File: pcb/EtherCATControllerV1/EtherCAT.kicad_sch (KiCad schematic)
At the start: 6 parts, among them U7 LAN9252/ML

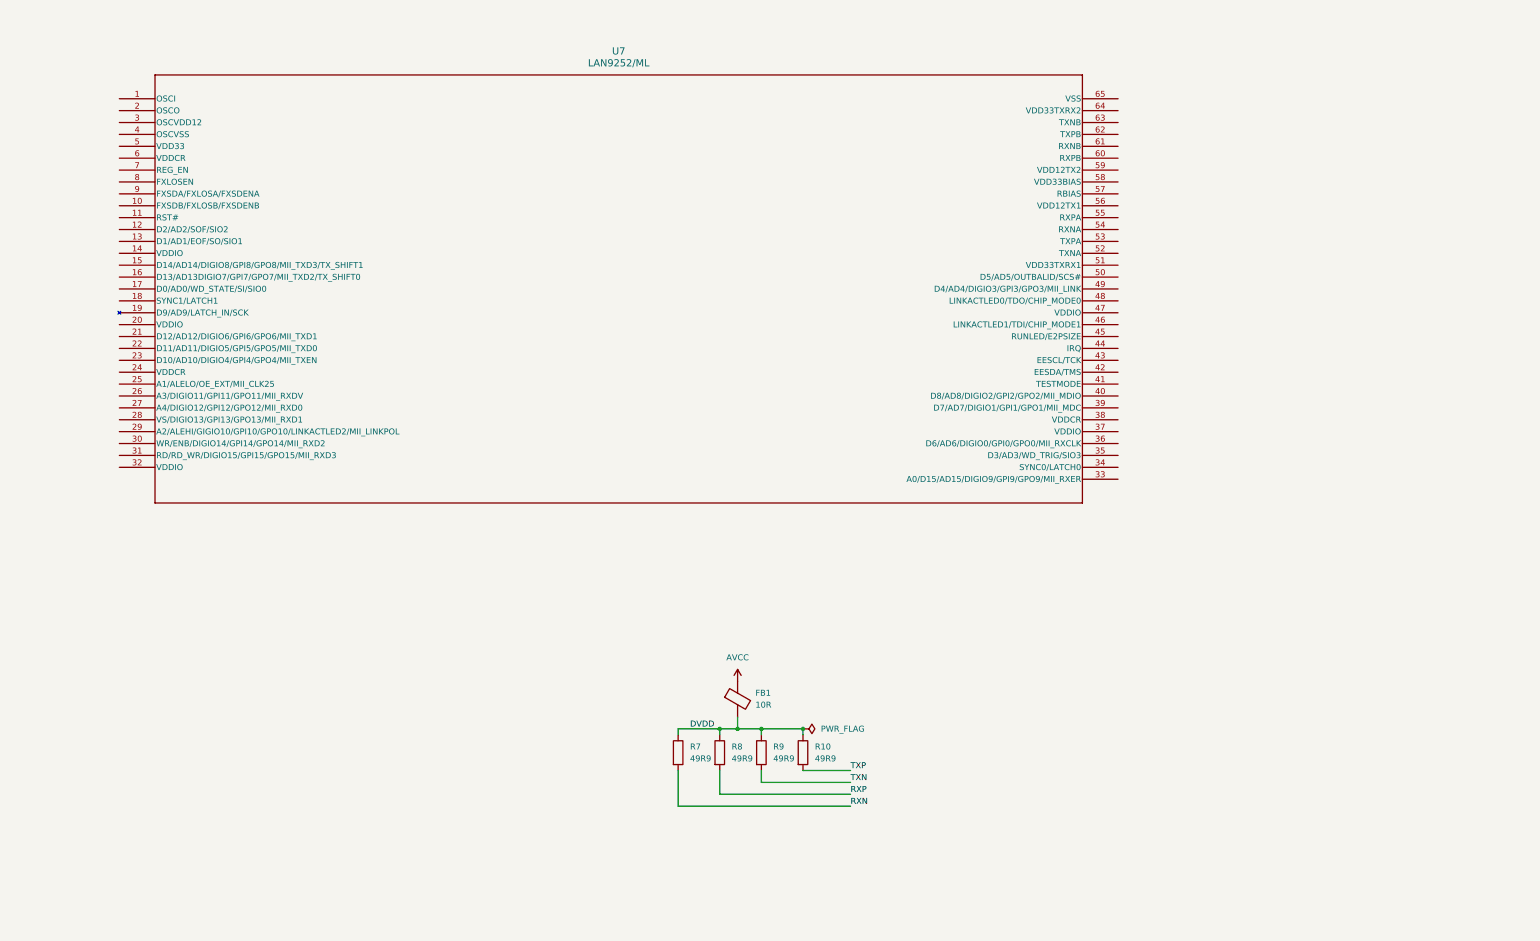
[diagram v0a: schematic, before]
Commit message: Initial design without Ethernet connectors
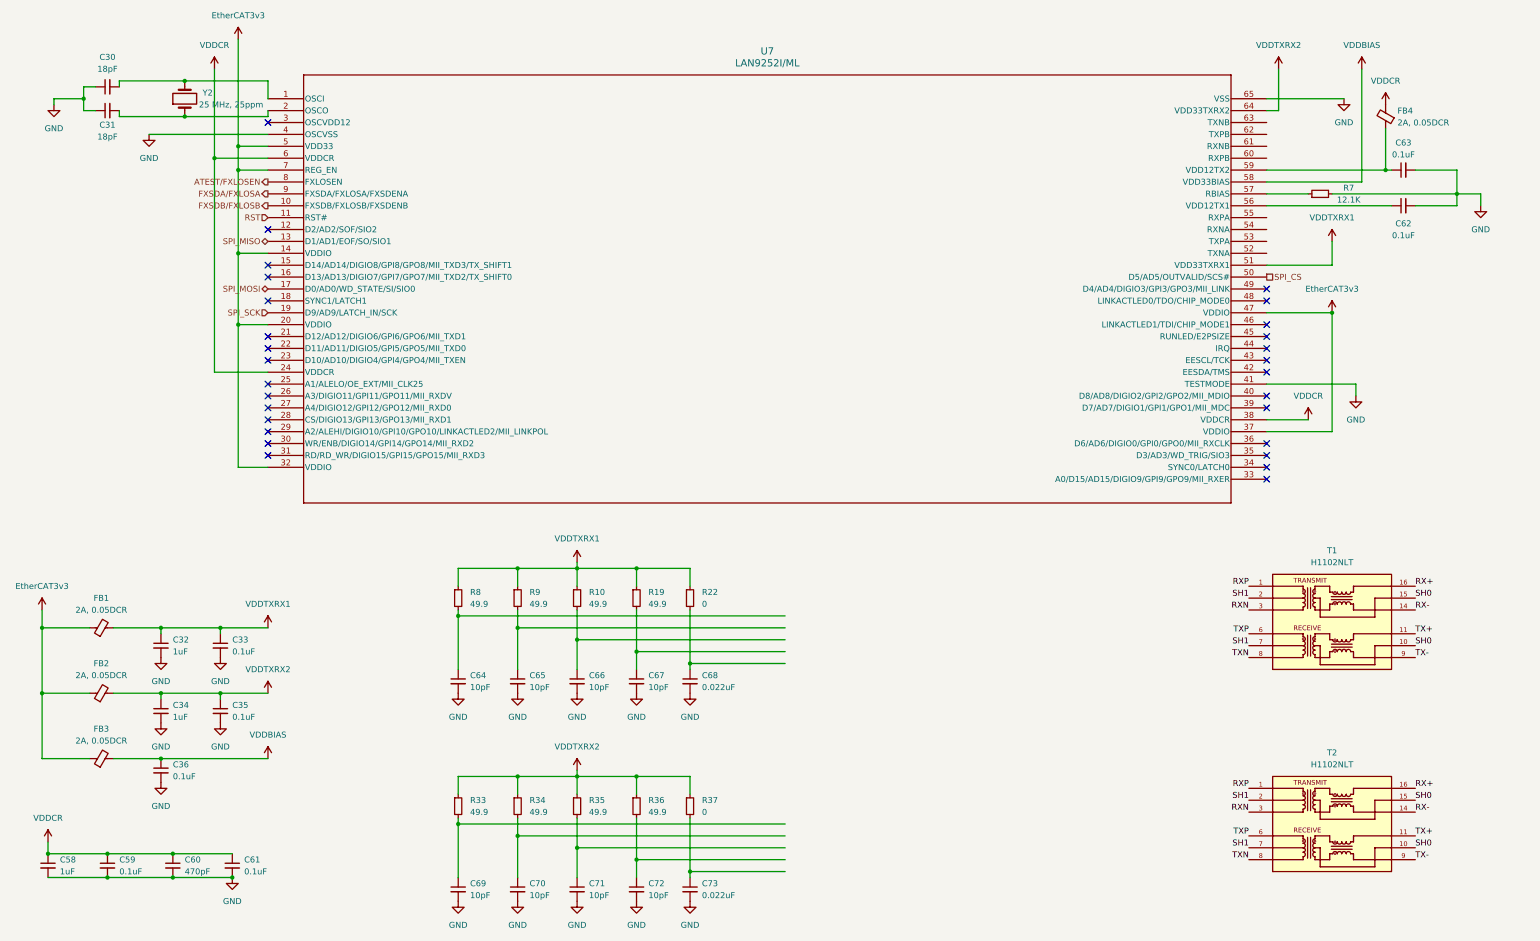
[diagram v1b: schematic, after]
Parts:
- removed FB1: 10R, Inductor_SMD:L_0402_1005Metric, symbol Device:FerriteBead
- removed R10, R7, R8, R9: 49R9, Resistor_SMD:R_0402_1005Metric, symbol Device:R
- removed U7: LAN9252/ML, QFN64_ML_MCH, symbol 2024-06-30_23-12-06:LAN9252_ML
- added C30, C31: 18pF, symbol Device:C_Small
- added C32, C34, C58: 1uF, symbol Device:C_Small
- added C33, C35, C36, C59, C61, C62, C63: 0.1uF, symbol Device:C_Small
- added C60: 470pF, symbol Device:C_Small
- added C64, C65, C66, C67, C69, C70, C71, C72: 10pF, symbol Device:C_Small
- added C68, C73: 0.022uF, symbol Device:C_Small
- added FB1, FB2, FB3, FB4: 2A, 0.05DCR, symbol Device:FerriteBead_Small
- added R10, R19, R33, R34, R35, R36, R8, R9: 49.9, symbol Device:R_Small
- added R22, R37: 0, symbol Device:R_Small
- added R7: 12.1K, symbol Device:R_Small
- added T1, T2: H1102NLT, Ethernet:XFMR_H1102NLT, symbol H1102NLT:H1102NLT
- added U7: LAN9252I/ML, QFN64_ML_MCH, symbol 2024-07-01_21-03-15:LAN9252I_ML
- added Y2: 25 MHz, 25ppm, symbol Device:Crystal
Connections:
- net RXN: now also T1.3, T2.3
- net RXP: now also T1.1, T2.1
- net TXN: now also T1.8, T2.8
- net TXP: now also T1.6, T2.6
- new net: C71.1, R35.2
- new net: C30.2, U7.1 (OSCI), Y2.2
- new net: C31.2, U7.2 (OSCO), Y2.1
- new net: C62.1, U7.56 (VDD12TX1)
- new net: R7.1, U7.57 (RBIAS)
- new net: C63.1, FB4.1, U7.59 (VDD12TX2)
- new net: C70.1, R34.2
- new net: C67.1, R19.2
- new net: C68.1, R22.2
- new net: C66.1, R10.2
- new net: C69.1, R33.2
- new net: C64.1, R8.2
- new net: C72.1, R36.2
- new net: C73.1, R37.2
- new net: C65.1, R9.2
- new net ATEST/FXLOSEN: U7.8 (FXLOSEN)
- new net EtherCAT3v3: FB1.1, FB2.1, FB3.1, U7.14 (VDDIO), U7.20 (VDDIO), U7.32 (VDDIO), U7.37 (VDDIO), U7.47 (VDDIO), U7.5 (VDD33), U7.7 (REG_EN)
- new net FXSDA/FXLOSA: U7.9 (FXSDA/FXLOSA/FXSDENA)
- new net FXSDB/FXLOSB: U7.10 (FXSDB/FXLOSB/FXSDENB)
- new net GND: C30.1, C31.1, C32.2, C33.2, C34.2, C35.2, C36.2, C58.2, C59.2, C60.2, C61.2, C62.2, C63.2, C64.2, C65.2, C66.2, C67.2, C68.2, C69.2, C70.2, C71.2, C72.2, C73.2, R7.2, U7.4 (OSCVSS), U7.41 (TESTMODE), U7.65 (VSS)
- new net RST: U7.11 (RST#)
- new net RX+: T1.16, T2.16
- new net RX-: T1.14, T2.14
- new net SH0: T1.10, T1.15, T2.10, T2.15
- new net SH1: T1.2, T1.7, T2.2, T2.7
- new net SPI_CS: U7.50 (D5/AD5/OUTVALID/SCS#)
- new net SPI_MISO: U7.13 (D1/AD1/EOF/SO/SIO1)
- new net SPI_MOSI: U7.17 (D0/AD0/WD_STATE/SI/SIO0)
- new net SPI_SCK: U7.19 (D9/AD9/LATCH_IN/SCK)
- new net TX+: T1.11, T2.11
- new net TX-: T1.9, T2.9
- new net VDDBIAS: C36.1, FB3.2, U7.58 (VDD33BIAS)
- new net VDDCR: C58.1, C59.1, C60.1, C61.1, FB4.2, U7.24 (VDDCR), U7.38 (VDDCR), U7.6 (VDDCR)
- new net VDDTXRX1: C32.1, C33.1, FB1.2, R10.1, R19.1, R22.1, R8.1, R9.1, U7.51 (VDD33TXRX1)
- new net VDDTXRX2: C34.1, C35.1, FB2.2, R33.1, R34.1, R35.1, R36.1, R37.1, U7.64 (VDD33TXRX2)
- no-connect marks 0 -> 28

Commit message: Added IO Board project
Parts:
- removed T1, T2: H1102NLT, Ethernet:XFMR_H1102NLT, symbol H1102NLT:H1102NLT
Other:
- note added: "EEPROM"

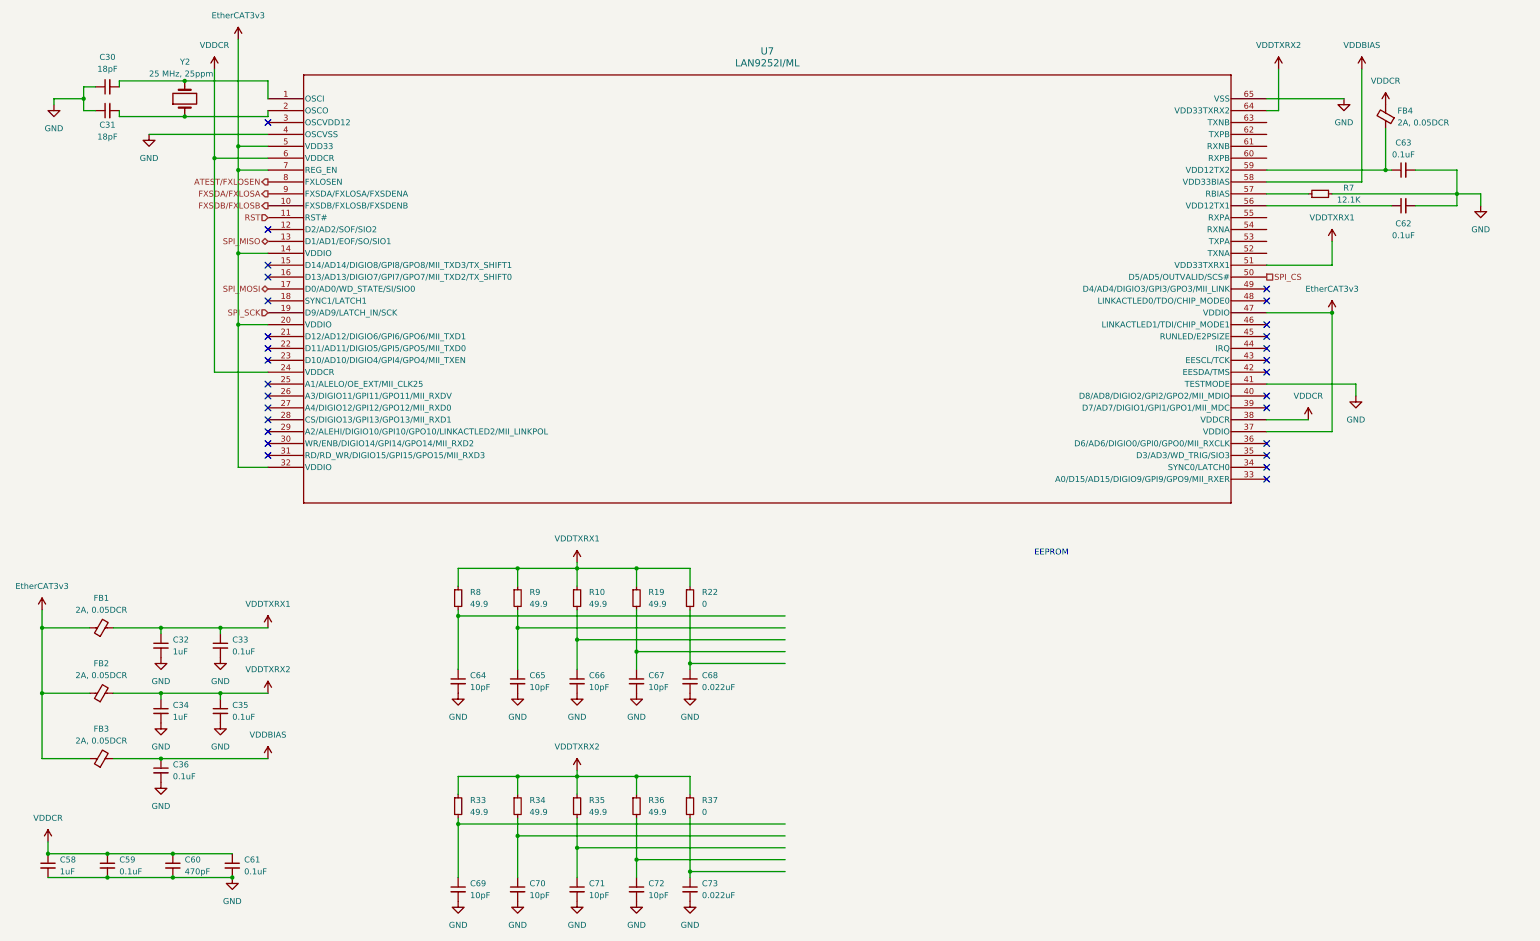
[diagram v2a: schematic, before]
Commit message: schematic finished, need to set proper ERCs
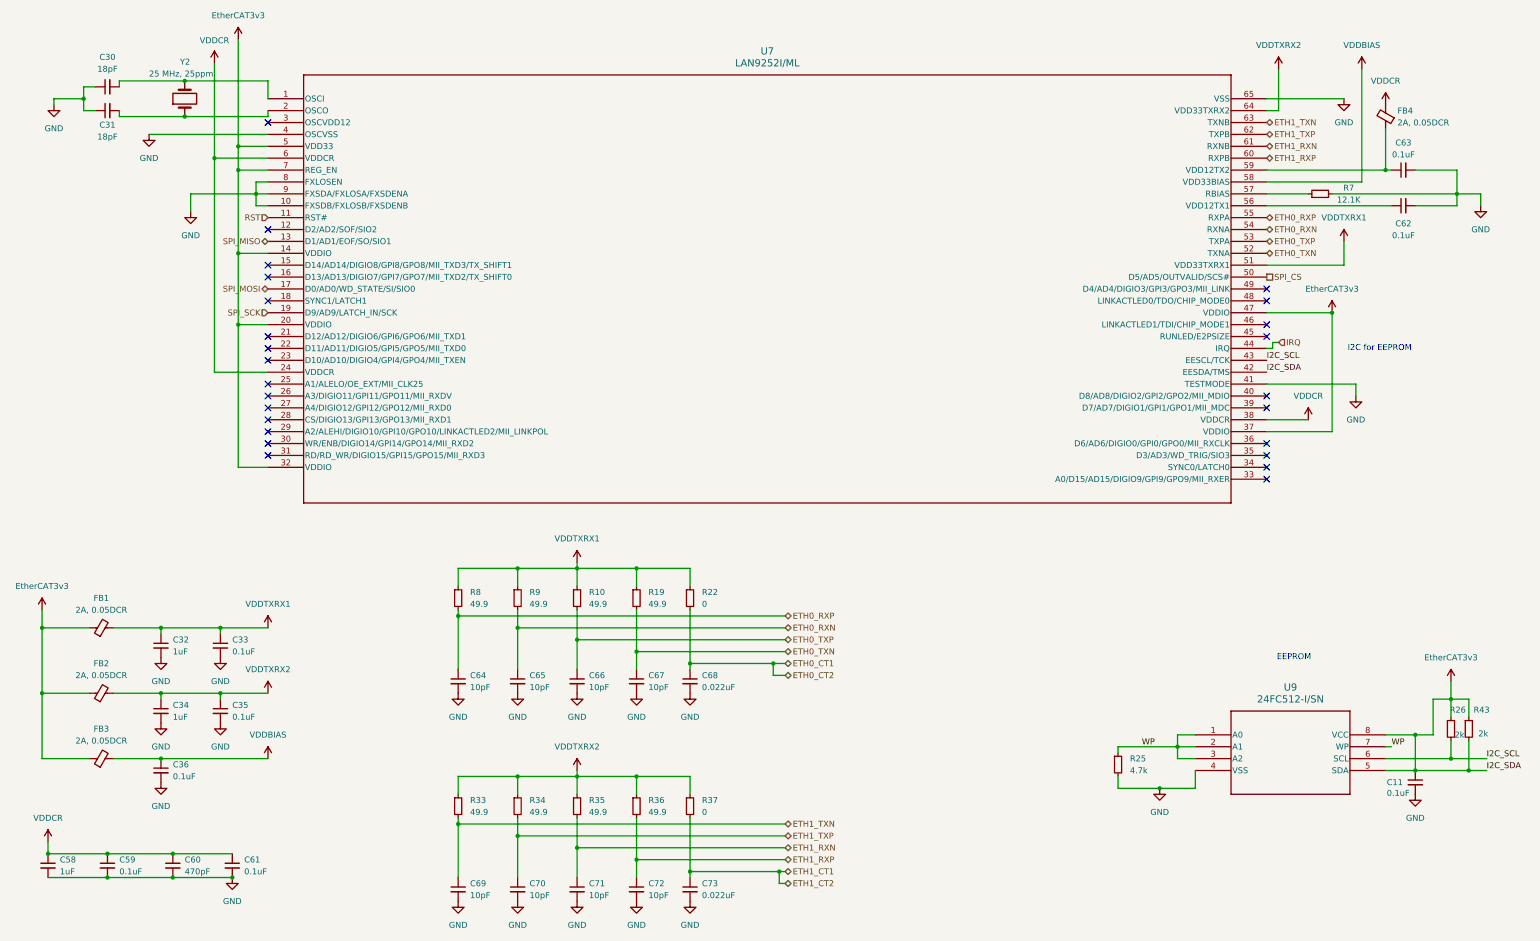
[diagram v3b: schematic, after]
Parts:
- added C11: 0.1uF, symbol Device:C_Small
- added R25: 4.7k, symbol Device:R_Small
- added R26, R43: 2k, symbol Device:R_Small
- added U9: 24FC512-I/SN, SOIC8_4P9X3P9MC_MCH, symbol 2024-07-03_18-39-37:24FC512-I_SN
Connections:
- net ATEST/FXLOSEN is gone; now on net GND: U7.8 (FXLOSEN)
- net FXSDA/FXLOSA is gone; now on net GND: U7.9 (FXSDA/FXLOSA/FXSDENA)
- net FXSDB/FXLOSB is gone; now on net GND: U7.10 (FXSDB/FXLOSB/FXSDENB)
- net EtherCAT3v3: now also U7.42 (EESDA/TMS), C11.1, R26.1, R43.1, R43.2, U9.5 (SDA), U9.8 (VCC)
- net GND: now also C11.2, R25.2, U9.4 (VSS)
- net ETH1_RXN: now reaches C71.1, R35.2
- net ETH1_RXN: now also U7.61 (RXNB)
- net I2C_SCL: now reaches U7.43 (EESCL/TCK)
- net I2C_SCL: now also R26.2, U9.6 (SCL)
- net IRQ: now reaches U7.44 (IRQ)
- net ETH0_TXN: now reaches U7.52 (TXNA)
- net ETH0_TXN: now also C67.1, R19.2
- net ETH0_TXP: now reaches U7.53 (TXPA)
- net ETH0_TXP: now also C66.1, R10.2
- net ETH0_RXN: now reaches U7.54 (RXNA)
- net ETH0_RXN: now also C65.1, R9.2
- net ETH0_RXP: now reaches U7.55 (RXPA)
- net ETH0_RXP: now also C64.1, R8.2
- net ETH1_RXP: now reaches U7.60 (RXPB)
- net ETH1_RXP: now also C72.1, R36.2
- net ETH1_TXP: now reaches U7.62 (TXPB)
- net ETH1_TXP: now also C70.1, R34.2
- net ETH1_TXN: now reaches U7.63 (TXNB)
- net ETH1_TXN: now also C69.1, R33.2
- net ETH0_CT1: now reaches C68.1, R22.2
- net ETH1_CT1: now reaches C73.1, R37.2
- new net WP: R25.1, U9.1 (A0), U9.2 (A1), U9.3 (A2), U9.7 (WP)
- no-connect marks 28 -> 25
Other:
- note added: "I2C for EEPROM"

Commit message: fix all ERCs
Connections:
- net at C62.1, U7.56 (VDD12TX1): now also C63.1, FB4.1, U7.59 (VDD12TX2)
